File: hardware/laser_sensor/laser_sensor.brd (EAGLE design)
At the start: 14 x 21 mm, 8 parts, among them J1 B4B-XH-A(LF)(SN), Q1 BC817-16LT1SMD

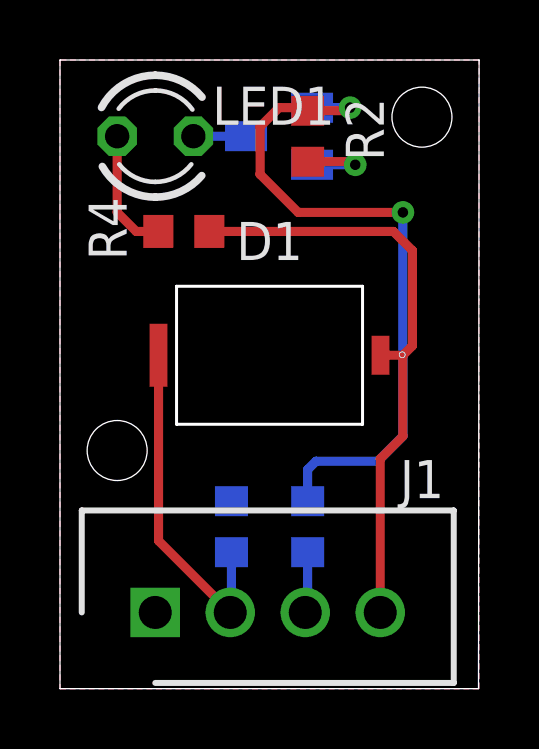
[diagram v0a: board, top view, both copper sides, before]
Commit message: changed some transistors
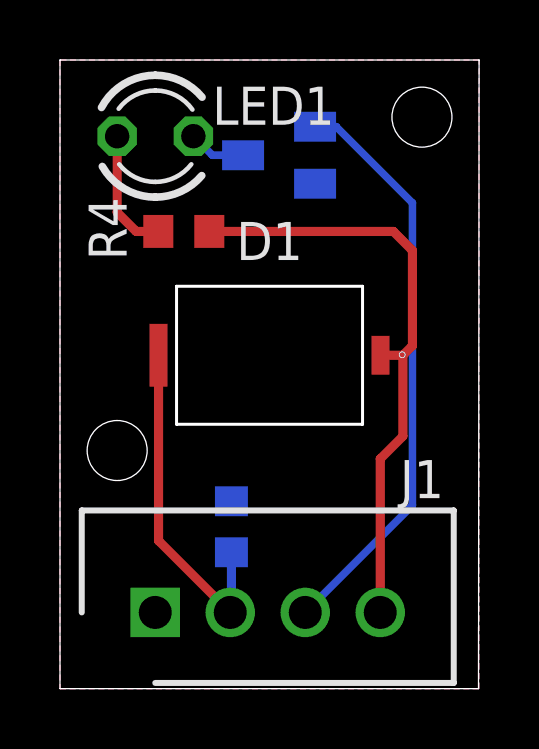
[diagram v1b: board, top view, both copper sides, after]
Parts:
- removed Q1: BC817-16LT1SMD, transistor-npn:SOT23-BEC
- removed R2: 100k, rcl:R0603
- removed R3: 10k, rcl:R0603
- added T1: (no value), transistor:SC59-BEC
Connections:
- removed net N$3: Q1.B, R2.1, R3.2
- net GND: now also T1.E; no longer Q1.E, R2.2
- net LED: now also T1.B; no longer R3.1
- net N$2: now also T1.C; no longer Q1.C
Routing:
- net N$3: track 23.6 -> 0.00 mm, vias 2 -> 0
- net LED: track 2.04 -> 19.4 mm
- net GND: track 3.07 -> 0.00 mm, vias 1 -> 0
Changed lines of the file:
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@@
 <dimension x1="0" y1="20.955" x2="13.97" y2="20.955" x3="6.985" y3="27.6225" textsize="1.778" layer="47"/>
 <dimension x1="0" y1="0" x2="6.985" y2="0" x3="3.4925" y3="23.495" textsize="1.778" layer="47"/>
-<text x="9.8425" y="4.445" size="1.778" layer="26" font="vector" rot="MR0">v1.0</text>
+<text x="12.7" y="4.1275" size="1.778" layer="26" font="vector" rot="MR0">v1.0</text>
 </plain>
 <attributes>
@@
 <attribute name="VALUE" x="5.08" y="16.764" size="1.27" layer="27" ratio="10"/>
 </element>
-<element name="Q1" library="transistor-npn" library_urn="urn:adsk.eagle:library:398" package="SOT23-BEC" package3d_urn="urn:adsk.eagle:package:28990/2" value="BC817-16LT1SMD" x="7.3025" y="18.415" smashed="yes" rot="MR270">
-<attribute name="NAME" x="5.3975" y="20.32" size="1.27" layer="26" rot="MR270"/>
-<attribute name="VALUE" x="10.4775" y="20.32" size="1.27" layer="28" rot="MR270"/>
-</element>
 <element name="R1" library="rcl" library_urn="urn:adsk.eagle:library:334" package="R0603" package3d_urn="urn:adsk.eagle:package:23555/2" value="100k" x="5.715" y="5.3975" smashed="yes" rot="MR90">
 <attribute name="NAME" x="3.175" y="4.445" size="1.27" layer="26" rot="MR90"/>
@@
 <attribute name="VALUE" x="3.175" y="4.1275" size="1.27" layer="28" rot="MR90"/>
 </element>
-<element name="R2" library="rcl" library_urn="urn:adsk.eagle:library:334" package="R0603" package3d_urn="urn:adsk.eagle:package:23555/2" value="100k" x="8.255" y="18.415" smashed="yes" rot="R270">
-<attribute name="NAME" x="9.525" y="19.685" size="1.27" layer="25" rot="R270"/>
-<attribute name="SPICEPREFIX" value="R" x="8.255" y="18.415" size="1.778" layer="27" rot="R270" display="off"/>
-<attribute name="VALUE" x="5.715" y="19.685" size="1.27" layer="27" rot="R270"/>
-</element>
-<element name="R3" library="rcl" library_urn="urn:adsk.eagle:library:334" package="R0603" package3d_urn="urn:adsk.eagle:package:23555/2" value="10k" x="8.255" y="5.3975" smashed="yes" rot="MR90">
-<attribute name="NAME" x="9.525" y="4.445" size="1.27" layer="26" rot="MR90"/>
-<attribute name="SPICEPREFIX" value="R" x="8.255" y="5.3975" size="1.778" layer="28" rot="MR90" display="off"/>
-<attribute name="VALUE" x="5.715" y="4.1275" size="1.27" layer="28" rot="MR90"/>
-</element>
 <element name="R4" library="rcl" library_urn="urn:adsk.eagle:library:334" package="R0603" package3d_urn="urn:adsk.eagle:package:23555/2" value="560" x="4.1275" y="15.24" smashed="yes">
 <attribute name="NAME" x="2.2225" y="14.2875" size="1.27" layer="25" rot="R90"/>
 <attribute name="SPICEPREFIX" value="R" x="4.1275" y="15.24" size="1.778" layer="27" display="off"/>
 <attribute name="VALUE" x="2.8575" y="12.7" size="1.27" layer="27"/>
+</element>
+<element name="T1" library="transistor" library_urn="urn:adsk.eagle:library:402" package="SC59-BEC" package3d_urn="urn:adsk.eagle:package:29926/2" value="" x="7.3025" y="17.78" smashed="yes" rot="MR270">
+<attribute name="NAME" x="9.525" y="17.4625" size="1.27" layer="26" rot="MR180"/>
+<attribute name="VALUE" x="10.4775" y="19.685" size="1.27" layer="28" rot="MR270"/>
 </element>
 </elements>
@@
 <contactref element="J1" pad="1"/>
 <contactref element="R1" pad="2"/>
-<contactref element="R2" pad="2"/>
-<contactref element="Q1" pad="E"/>
-<wire x1="8.4025" y1="17.465" x2="8.405" y2="17.4625" width="0.3048" layer="16"/>
-<wire x1="8.405" y1="17.4625" x2="9.8425" y2="17.4625" width="0.3048" layer="16"/>
-<via x="9.8425" y="17.4625" extent="1-16" drill="0.35"/>
-<wire x1="9.8425" y1="17.4625" x2="9.74" y2="17.565" width="0.3048" layer="1"/>
-<wire x1="9.74" y1="17.565" x2="8.255" y2="17.565" width="0.3048" layer="1"/>
 <polygon width="0.3048" layer="1">
 <vertex x="13.97" y="20.955"/>
@@
 <vertex x="13.97" y="0"/>
 </polygon>
+<contactref element="T1" pad="E"/>
 </signal>
 <signal name="+5V">
@@
 <signal name="LED">
 <contactref element="J1" pad="3"/>
-<contactref element="R3" pad="1"/>
-<wire x1="8.175" y1="2.54" x2="8.255" y2="2.62" width="0.3048" layer="16"/>
-<wire x1="8.255" y1="2.62" x2="8.255" y2="4.5475" width="0.3048" layer="16"/>
+<contactref element="T1" pad="B"/>
+<wire x1="8.175" y1="2.54" x2="11.7475" y2="6.1125" width="0.254" layer="16"/>
+<wire x1="11.7475" y1="16.1925" x2="9.2075" y2="18.7325" width="0.254" layer="16"/>
+<wire x1="9.2075" y1="18.7325" x2="9.205" y2="18.73" width="0.254" layer="16"/>
+<wire x1="9.205" y1="18.73" x2="8.5025" y2="18.73" width="0.254" layer="16"/>
+<wire x1="11.7475" y1="6.1125" x2="11.7475" y2="16.1925" width="0.254" layer="16"/>
 </signal>
 <signal name="N$1">
@@
 </signal>
 <signal name="N$2">
+<contactref element="T1" pad="C"/>
 <contactref element="LED1" pad="K"/>
-<contactref element="Q1" pad="C"/>
-<wire x1="6.2025" y1="18.415" x2="4.445" y2="18.415" width="0.3048" layer="16"/>
-</signal>
-<signal name="N$3">
-<contactref element="Q1" pad="B"/>
-<contactref element="R3" pad="2"/>
-<contactref element="R2" pad="1"/>
-<wire x1="8.4025" y1="19.365" x2="8.405" y2="19.3675" width="0.3048" layer="16"/>
-<wire x1="8.405" y1="19.3675" x2="9.6708" y2="19.3675" width="0.3048" layer="16"/>
-<via x="9.6708" y="19.3675" extent="1-16" drill="0.35"/>
-<wire x1="9.6708" y1="19.3675" x2="9.5683" y2="19.265" width="0.3048" layer="1"/>
-<wire x1="9.5683" y1="19.265" x2="8.255" y2="19.265" width="0.3048" layer="1"/>
-<wire x1="8.255" y1="7.3025" x2="8.5331" y2="7.5806" width="0.3048" layer="16"/>
-<wire x1="8.255" y1="6.2475" x2="8.255" y2="7.3025" width="0.3048" layer="16"/>
-<wire x1="8.5331" y1="7.5806" x2="10.595275" y2="7.5806" width="0.3048" layer="16"/>
-<wire x1="10.595275" y1="7.5806" x2="11.43" y2="8.415325" width="0.3048" layer="16"/>
-<wire x1="11.43" y1="8.415325" x2="11.43" y2="15.875" width="0.3048" layer="16"/>
-<via x="11.43" y="15.875" extent="1-16" drill="0.35"/>
-<wire x1="11.43" y1="15.875" x2="7.9375" y2="15.875" width="0.3048" layer="1"/>
-<wire x1="7.9375" y1="15.875" x2="6.6675" y2="17.145" width="0.3048" layer="1"/>
-<wire x1="6.6675" y1="17.145" x2="6.6675" y2="18.7325" width="0.3048" layer="1"/>
-<wire x1="6.6675" y1="18.7325" x2="7.3025" y2="19.3675" width="0.3048" layer="1"/>
-<wire x1="7.3025" y1="19.3675" x2="8.1525" y2="19.3675" width="0.3048" layer="1"/>
-<wire x1="8.1525" y1="19.3675" x2="8.255" y2="19.265" width="0.3048" layer="1"/>
+<wire x1="6.1025" y1="17.78" x2="5.08" y2="17.78" width="0.254" layer="16"/>
+<wire x1="5.08" y1="17.78" x2="4.445" y2="18.415" width="0.254" layer="16"/>
 </signal>
 </signals>
